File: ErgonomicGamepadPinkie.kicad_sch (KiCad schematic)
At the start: 11 parts, among them J2 Conn_01x05, SW3 SW_DIP_x01, SW5 SW_DIP_x01, SW6 SW_DIP_x01, SW7 SW_DIP_x01, SW8 SW_DIP_x01

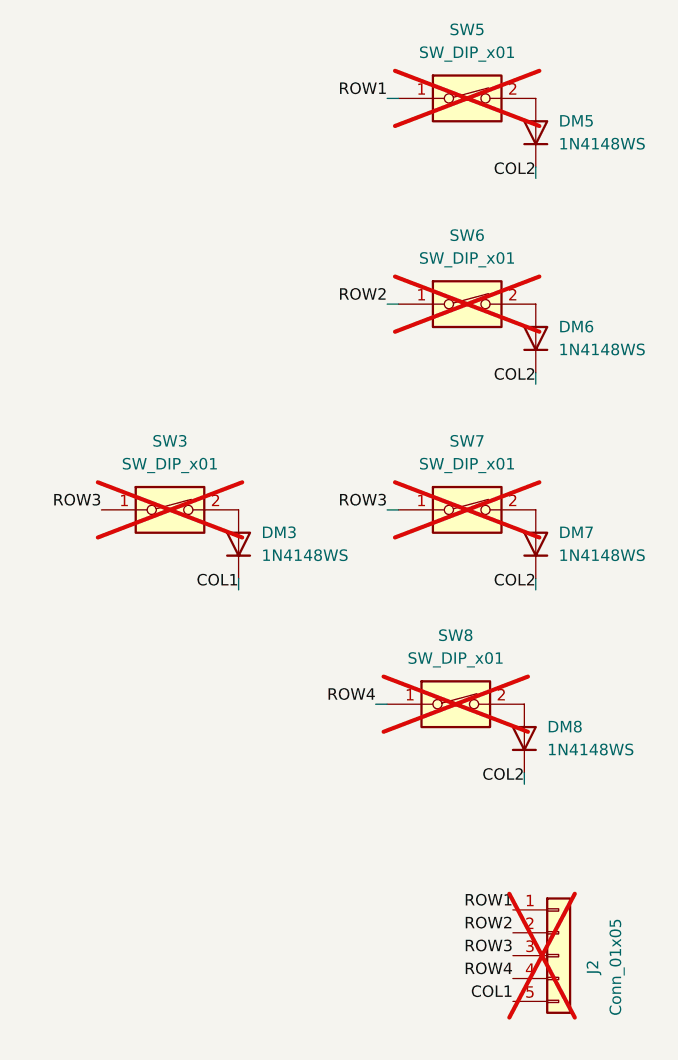
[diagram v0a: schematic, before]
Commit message: Continue ergonomic key stagger adjustments across satellite sheets
Update the layout-mirror script to read symbol positions from every
kicad_sch in the project, since the key matrix now lives across the
Pinkie/Thumb satellite sheets rather than a single top-level sheet.
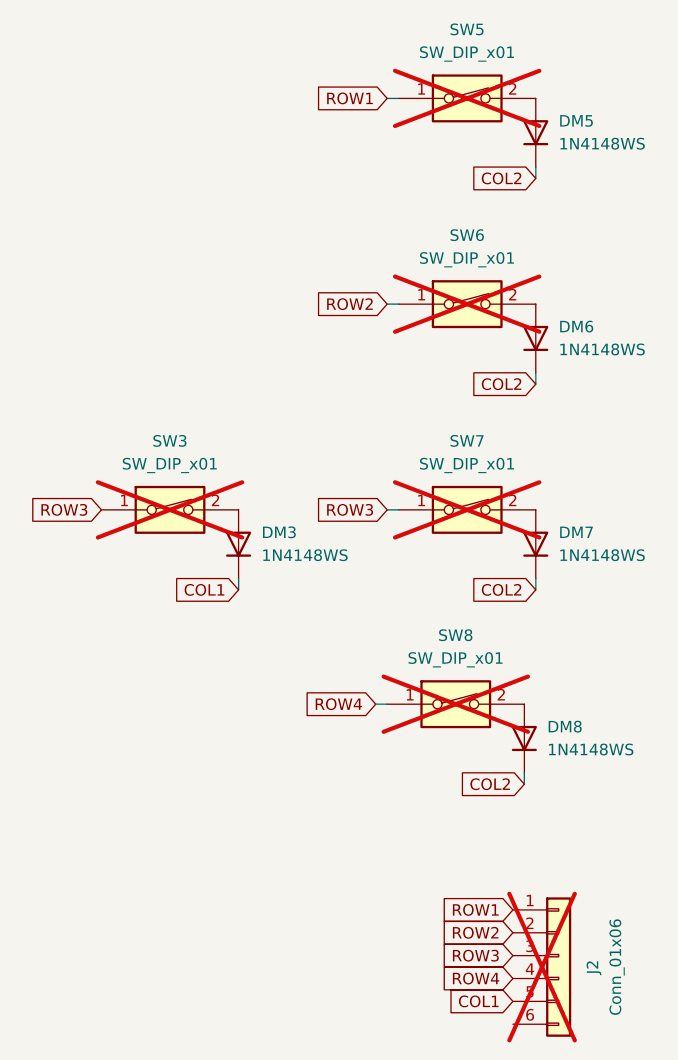
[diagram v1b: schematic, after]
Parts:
- J2: value Conn_01x05 -> Conn_01x06; footprint Connector_JST:JST_XH_B5B-XH-A_1x05_P2.50mm_Vertical -> Connector_JST:JST_XH_B6B-XH-A_1x06_P2.50mm_Vertical; symbol Connector_Generic:Conn_01x05 -> Connector_Generic:Conn_01x06; LCSC C157991 -> C144397; MPN B5B-XH-A(LF)(SN) -> B6B-XH-A(LF)(SN)
